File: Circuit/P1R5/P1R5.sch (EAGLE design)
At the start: 181 parts, among them J1 2X5_0.05"_CORTEX_DEBUGTH_NOKE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, U1 MK20DX256VLH7, U2 TPS61200, U3 PCA9552BS, U4 PCA9552BS, U5 MPU-9250, U6 ESP8266EX, U7 25Q40, U8 NRF24L01, Y1 8MHz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

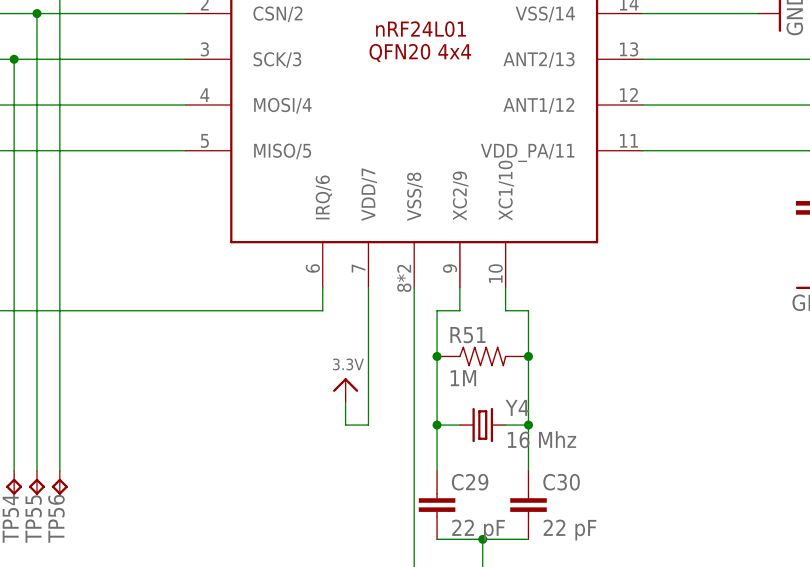
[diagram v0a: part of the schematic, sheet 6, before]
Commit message: Updated footprint for mesh after reviewing datasheet and finding a recommendation to not connect the ground pad.
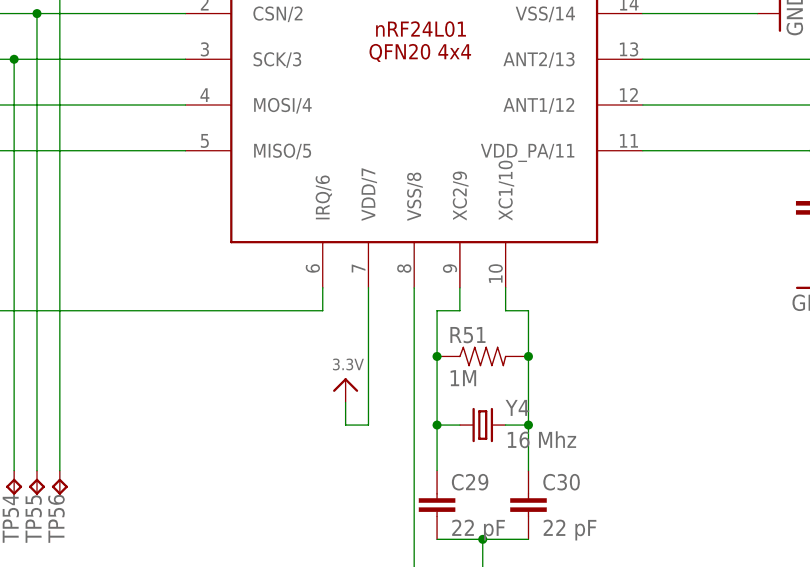
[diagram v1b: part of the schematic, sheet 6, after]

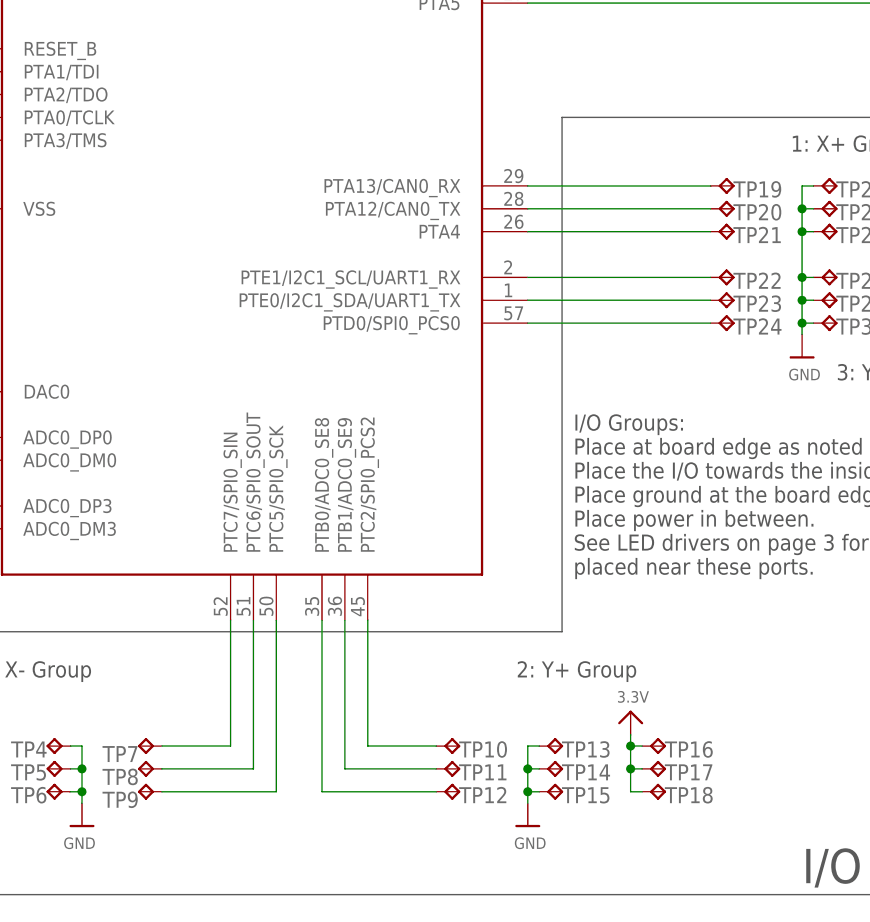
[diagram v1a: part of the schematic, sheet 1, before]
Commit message: Added port numbers to schematic.
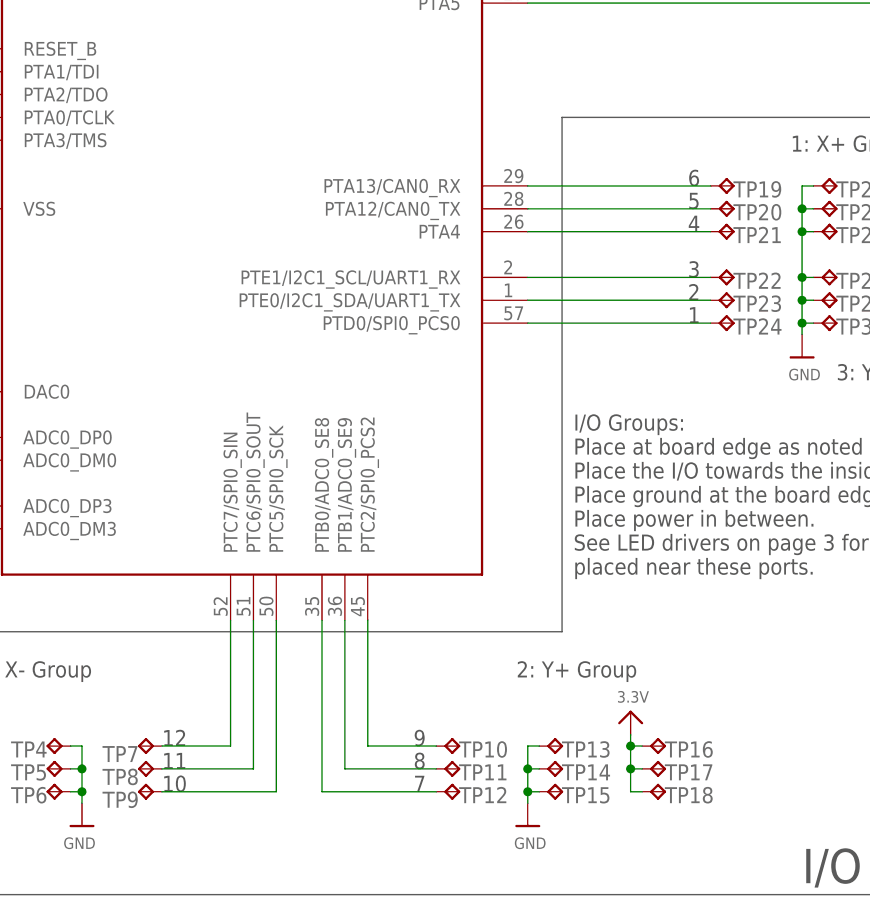
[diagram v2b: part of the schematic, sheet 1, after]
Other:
- note added: "1"
- note added: "10"
- note added: "11"
- note added: "12"
- note added: "2"
- note added: "3"
- note added: "4"
- note added: "5"
- note added: "6"
- note added: "7"
- note added: "8"
- note added: "9"
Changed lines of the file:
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@@
 <setting verticaltext="up"/>
 </settings>
-<grid distance="0.1" unitdist="inch" unit="inch" style="lines" multiple="1" display="no" altdistance="0.01" altunitdist="inch" altunit="inch"/>
+<grid distance="0.05" unitdist="inch" unit="inch" style="lines" multiple="1" display="no" altdistance="0.01" altunitdist="inch" altunit="inch"/>
 <layers>
 <layer number="1" name="Top" color="4" fill="1" visible="no" active="no"/>
@@
 <text x="321.31" y="-182.88" size="2.54" layer="97" rot="R180">To LEDs, page 3</text>
 <text x="313.69" y="-170.18" size="2.54" layer="97">To LEDs on page 3 and IMU on page 4</text>
+<text x="161.29" y="-266.7" size="1.778" layer="97">10</text>
+<text x="161.29" y="-264.16" size="1.778" layer="97">11</text>
+<text x="161.29" y="-261.62" size="1.778" layer="97">12</text>
+<text x="189.23" y="-261.62" size="1.778" layer="97">9</text>
+<text x="189.23" y="-264.16" size="1.778" layer="97">8</text>
+<text x="189.23" y="-266.7" size="1.778" layer="97">7</text>
+<text x="219.71" y="-199.39" size="1.778" layer="97">6</text>
+<text x="219.71" y="-201.93" size="1.778" layer="97">5</text>
+<text x="219.71" y="-204.47" size="1.778" layer="97">4</text>
+<text x="219.71" y="-209.55" size="1.778" layer="97">3</text>
+<text x="219.71" y="-212.09" size="1.778" layer="97">2</text>
+<text x="219.71" y="-214.63" size="1.778" layer="97">1</text>
 </plain>
 <instances>

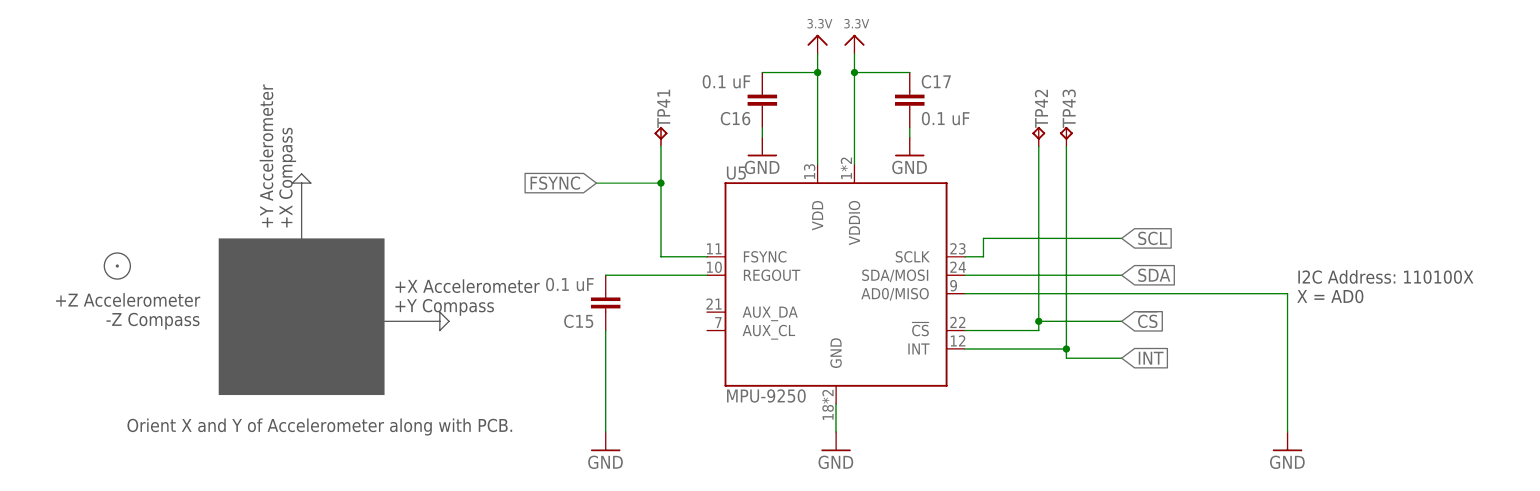
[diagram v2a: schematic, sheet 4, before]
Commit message: Updated Clay 5 firmware. Added the Messenger interface for remote terminal access and processing of text messages.
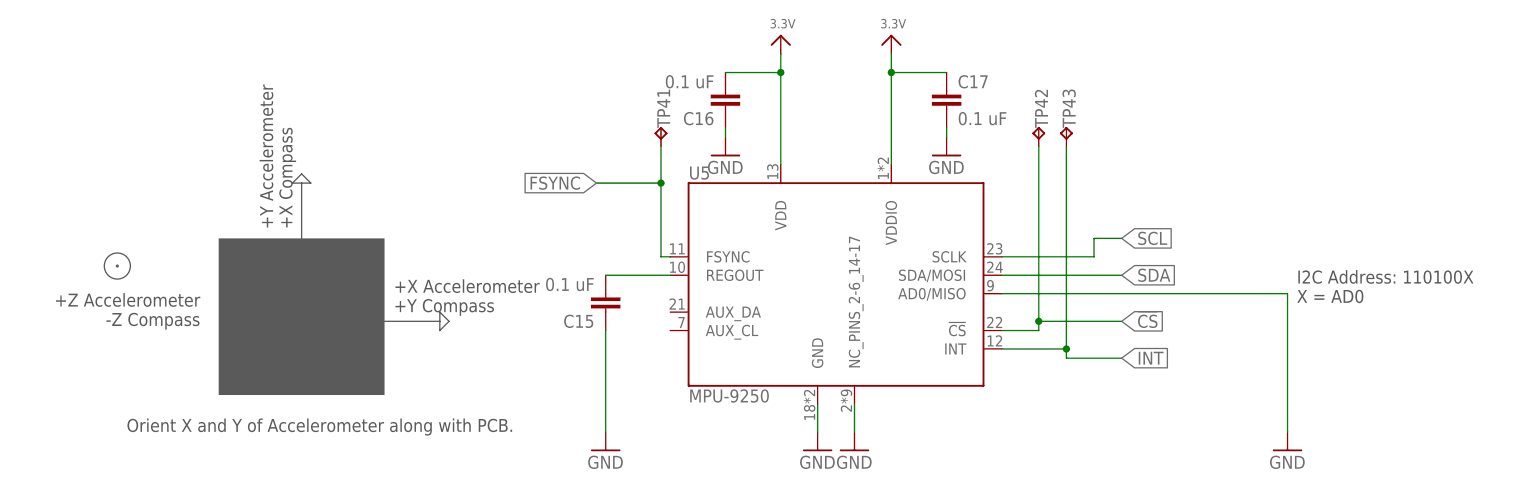
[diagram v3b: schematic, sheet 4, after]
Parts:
- JP1: PARTNO M20PTH -> S2B-PH-K-S(LF)(SN)
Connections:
- net GND: now also U5.NC_PINS_2-6_14-17
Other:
- moved on the sheet: C16, C17
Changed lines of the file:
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@@
 </part>
 <part name="JP1" library="SparkFun-Connectors" deviceset="M02" device="PTH" value="M20PTH">
-<attribute name="PARTNO" value="M20PTH"/>
+<attribute name="PARTNO" value="S2B-PH-K-S(LF)(SN)"/>
 </part>
 <part name="S1" library="SparkFun-Electromechanical" deviceset="SWITCH-SPDT" device="-SMD-A" value="CUS-12TB">
@@
 <part name="GND25" library="supply1" deviceset="GND" device=""/>
 <part name="_2" library="microbuilder" deviceset="GND" device=""/>
+<part name="GND47" library="SparkFun" deviceset="GND" device=""/>
 </parts>
 <sheets>
@@
 <attribute name="PARTNO" x="123.19" y="-82.55" size="1.778" layer="96" display="off"/>
 </instance>
-<instance part="C16" gate="G$1" x="113.03" y="-54.61" rot="R180">
-<attribute name="PARTNO" x="113.03" y="-54.61" size="1.778" layer="96" display="off"/>
+<instance part="C16" gate="G$1" x="107.95" y="-54.61" rot="R180">
+<attribute name="PARTNO" x="107.95" y="-54.61" size="1.778" layer="96" display="off"/>
 </instance>
-<instance part="C17" gate="G$1" x="133.35" y="-57.15">
-<attribute name="PARTNO" x="133.35" y="-57.15" size="1.778" layer="96" display="off"/>
+<instance part="C17" gate="G$1" x="138.43" y="-57.15">
+<attribute name="PARTNO" x="138.43" y="-57.15" size="1.778" layer="96" display="off"/>
 </instance>
 <instance part="C15" gate="G$1" x="91.44" y="-82.55" rot="R180">
 <attribute name="PARTNO" x="91.44" y="-82.55" size="1.778" layer="96" display="off"/>
 </instance>
-<instance part="GND20" gate="1" x="123.19" y="-104.14"/>
-<instance part="GND19" gate="1" x="113.03" y="-63.5"/>
-<instance part="GND21" gate="1" x="133.35" y="-63.5"/>
+<instance part="GND20" gate="1" x="120.65" y="-104.14"/>
+<instance part="GND19" gate="1" x="107.95" y="-63.5"/>
+<instance part="GND21" gate="1" x="138.43" y="-63.5"/>
 <instance part="GND18" gate="1" x="91.44" y="-104.14"/>
 <instance part="GND22" gate="1" x="185.42" y="-104.14"/>
-<instance part="_39" gate="G$1" x="120.65" y="-46.99"/>
-<instance part="_40" gate="G$1" x="125.73" y="-46.99"/>
+<instance part="_39" gate="G$1" x="115.57" y="-46.99"/>
+<instance part="_40" gate="G$1" x="130.81" y="-46.99"/>
 <instance part="TP43" gate="G$1" x="154.94" y="-59.69" smashed="yes">
 <attribute name="NAME" x="156.21" y="-59.69" size="1.778" layer="95" rot="R90"/>
@@
 <attribute name="PARTNO" x="151.13" y="-59.69" size="1.778" layer="96" rot="R90" display="off"/>
 </instance>
+<instance part="GND47" gate="1" x="125.73" y="-104.14"/>
 </instances>
 <busses>
@@
 <pinref part="U5" gate="G$1" pin="SDA/MOSI"/>
 <label x="162.56" y="-80.01" size="1.778" layer="95" xref="yes"/>
-<wire x1="140.97" y1="-80.01" x2="162.56" y2="-80.01" width="0.1524" layer="91"/>
+<wire x1="146.05" y1="-80.01" x2="162.56" y2="-80.01" width="0.1524" layer="91"/>
 </segment>
 </net>
@@
 <wire x1="90.17" y1="-67.31" x2="99.06" y2="-67.31" width="0.1524" layer="91"/>
 <wire x1="99.06" y1="-67.31" x2="99.06" y2="-77.47" width="0.1524" layer="91"/>
-<wire x1="99.06" y1="-77.47" x2="105.41" y2="-77.47" width="0.1524" layer="91"/>
+<wire x1="99.06" y1="-77.47" x2="100.33" y2="-77.47" width="0.1524" layer="91"/>
 <pinref part="TP41" gate="G$1" pin="TP"/>
 <wire x1="99.06" y1="-67.31" x2="99.06" y2="-62.23" width="0.1524" layer="91"/>
@@
 <net name="N$4" class="0">
 <segment>
-<wire x1="105.41" y1="-80.01" x2="91.44" y2="-80.01" width="0.1524" layer="91"/>
+<wire x1="100.33" y1="-80.01" x2="91.44" y2="-80.01" width="0.1524" layer="91"/>
 <pinref part="U5" gate="G$1" pin="REGOUT"/>
 <pinref part="C15" gate="G$1" pin="2"/>
@@
 <pinref part="U5" gate="G$1" pin="INT"/>
 <label x="162.56" y="-91.44" size="1.778" layer="95" xref="yes"/>
-<wire x1="140.97" y1="-90.17" x2="154.94" y2="-90.17" width="0.1524" layer="91"/>
+<wire x1="146.05" y1="-90.17" x2="154.94" y2="-90.17" width="0.1524" layer="91"/>
 <wire x1="154.94" y1="-90.17" x2="154.94" y2="-91.44" width="0.1524" layer="91"/>
 <wire x1="154.94" y1="-91.44" x2="162.56" y2="-91.44" width="0.1524" layer="91"/>
@@
 </segment>
 <segment>
-<wire x1="123.19" y1="-97.79" x2="123.19" y2="-101.6" width="0.1524" layer="91"/>
+<wire x1="120.65" y1="-97.79" x2="120.65" y2="-101.6" width="0.1524" layer="91"/>
 <pinref part="U5" gate="G$1" pin="GND"/>
 <pinref part="GND20" gate="1" pin="GND"/>
 </segment>
 <segment>
-<wire x1="113.03" y1="-59.69" x2="113.03" y2="-60.96" width="0.1524" layer="91"/>
+<wire x1="107.95" y1="-59.69" x2="107.95" y2="-60.96" width="0.1524" layer="91"/>
 <pinref part="C16" gate="G$1" pin="1"/>
 <pinref part="GND19" gate="1" pin="GND"/>
 </segment>
 <segment>
-<wire x1="133.35" y1="-59.69" x2="133.35" y2="-60.96" width="0.1524" layer="91"/>
+<wire x1="138.43" y1="-59.69" x2="138.43" y2="-60.96" width="0.1524" layer="91"/>
 <pinref part="C17" gate="G$1" pin="2"/>
 <pinref part="GND21" gate="1" pin="GND"/>
@@
 <wire x1="185.42" y1="-82.55" x2="185.42" y2="-101.6" width="0.1524" layer="91"/>
 <pinref part="U5" gate="G$1" pin="AD0/MISO"/>
-<wire x1="140.97" y1="-82.55" x2="185.42" y2="-82.55" width="0.1524" layer="91"/>
+<wire x1="146.05" y1="-82.55" x2="185.42" y2="-82.55" width="0.1524" layer="91"/>
+</segment>
+<segment>
+<pinref part="U5" gate="G$1" pin="NC_PINS_2-6_14-17"/>
+<pinref part="GND47" gate="1" pin="GND"/>
+<wire x1="125.73" y1="-97.79" x2="125.73" y2="-101.6" width="0.1524" layer="91"/>
 </segment>
 </net>
@@
 <segment>
 <pinref part="U5" gate="G$1" pin="SCLK"/>
-<wire x1="140.97" y1="-77.47" x2="143.51" y2="-77.47" width="0.1524" layer="91"/>
+<wire x1="146.05" y1="-77.47" x2="158.75" y2="-77.47" width="0.1524" layer="91"/>
 <label x="162.56" y="-74.93" size="1.778" layer="95" xref="yes"/>
-<wire x1="143.51" y1="-77.47" x2="143.51" y2="-74.93" width="0.1524" layer="91"/>
-<wire x1="143.51" y1="-74.93" x2="162.56" y2="-74.93" width="0.1524" layer="91"/>
+<wire x1="158.75" y1="-77.47" x2="158.75" y2="-74.93" width="0.1524" layer="91"/>
+<wire x1="158.75" y1="-74.93" x2="162.56" y2="-74.93" width="0.1524" layer="91"/>
 </segment>
 </net>
@@
 <segment>
 <pinref part="U5" gate="G$1" pin="!CS"/>
-<wire x1="140.97" y1="-87.63" x2="151.13" y2="-87.63" width="0.1524" layer="91"/>
+<wire x1="146.05" y1="-87.63" x2="151.13" y2="-87.63" width="0.1524" layer="91"/>
 <wire x1="151.13" y1="-87.63" x2="151.13" y2="-86.36" width="0.1524" layer="91"/>
 <wire x1="151.13" y1="-86.36" x2="162.56" y2="-86.36" width="0.1524" layer="91"/>
@@
 <pinref part="C16" gate="G$1" pin="2"/>
 <pinref part="U5" gate="G$1" pin="VDD"/>
-<wire x1="120.65" y1="-64.77" x2="120.65" y2="-52.07" width="0.1524" layer="91"/>
-<wire x1="120.65" y1="-52.07" x2="113.03" y2="-52.07" width="0.1524" layer="91"/>
-<wire x1="120.65" y1="-49.53" x2="120.65" y2="-52.07" width="0.1524" layer="91"/>
-<junction x="120.65" y="-52.07"/>
+<wire x1="115.57" y1="-64.77" x2="115.57" y2="-52.07" width="0.1524" layer="91"/>
+<wire x1="115.57" y1="-52.07" x2="107.95" y2="-52.07" width="0.1524" layer="91"/>
+<wire x1="115.57" y1="-49.53" x2="115.57" y2="-52.07" width="0.1524" layer="91"/>
+<junction x="115.57" y="-52.07"/>
 <pinref part="_39" gate="G$1" pin="3.3V"/>
 </segment>
@@
 <pinref part="U5" gate="G$1" pin="VDDIO"/>
 <pinref part="C17" gate="G$1" pin="1"/>
-<wire x1="125.73" y1="-49.53" x2="125.73" y2="-52.07" width="0.1524" layer="91"/>
-<wire x1="125.73" y1="-52.07" x2="133.35" y2="-52.07" width="0.1524" layer="91"/>
-<wire x1="125.73" y1="-64.77" x2="125.73" y2="-52.07" width="0.1524" layer="91"/>
-<junction x="125.73" y="-52.07"/>
+<wire x1="130.81" y1="-49.53" x2="130.81" y2="-52.07" width="0.1524" layer="91"/>
+<wire x1="130.81" y1="-52.07" x2="138.43" y2="-52.07" width="0.1524" layer="91"/>
+<wire x1="130.81" y1="-64.77" x2="130.81" y2="-52.07" width="0.1524" layer="91"/>
+<junction x="130.81" y="-52.07"/>
 <pinref part="_40" gate="G$1" pin="3.3V"/>
 </segment>
